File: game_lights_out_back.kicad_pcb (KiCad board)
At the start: 2 copper layers, 171 x 131.3 mm, 6 parts

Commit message: Added game legend
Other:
- board text added: "EASY"
- board text added: "HARD"
- board text added: "MAD"
- board text added: "MODE"
- board text added: "PATTERN"
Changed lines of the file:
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@@
     (pad "1" thru_hole circle (at 0 0) (size 5.6 5.6) (drill 3.2) (layers "*.Cu" "*.Mask"))
   )
+  (gr_circle (center 90.543571 118.5) (end 88.718571 119.325)
+    (stroke (width 0.32) (type default)) (fill none) (layer "B.SilkS"))
+  (gr_circle (center 70.6525 124.8) (end 69.8275 122.975)
+    (stroke (width 0.32) (type default)) (fill solid) (layer "B.SilkS"))
+  (gr_circle (center 99.787166 95.025) (end 97.962166 95.85)
+    (stroke (width 0.32) (type default)) (fill none) (layer "B.SilkS"))
+  (gr_circle (center 135.634643 118.5) (end 134.809643 116.675)
+    (stroke (width 0.32) (type default)) (fill solid) (layer "B.SilkS"))
+  (gr_circle (center 123.034643 124.8) (end 121.209643 125.625)
+    (stroke (width 0.32) (type default)) (fill none) (layer "B.SilkS"))
+  (gr_circle (center 93.814976 95.025) (end 91.989976 95.85)
+    (stroke (width 0.15) (type default)) (fill solid) (layer "B.SilkS"))
+  (gr_circle (center 96.843571 118.5) (end 95.018571 119.325)
+    (stroke (width 0.32) (type default)) (fill solid) (layer "B.SilkS"))
+  (gr_circle (center 58.0525 112.2) (end 56.2275 113.025)
+    (stroke (width 0.32) (type default)) (fill solid) (layer "B.SilkS"))
+  (gr_circle (center 64.3525 124.8) (end 62.5275 125.625)
+    (stroke (width 0.32) (type default)) (fill none) (layer "B.SilkS"))
+  (gr_circle (center 61.366405 95.11) (end 59.541405 95.935)
+    (stroke (width 0.15) (type default)) (fill solid) (layer "B.SilkS"))
+  (gr_circle (center 129.334643 124.8) (end 127.509643 125.625)
+    (stroke (width 0.32) (type default)) (fill none) (layer "B.SilkS"))
+  (gr_circle (center 103.143571 124.8) (end 102.318571 122.975)
+    (stroke (width 0.32) (type default)) (fill solid) (layer "B.SilkS"))
+  (gr_line (start 176.7175 106.025) (end 49.5025 106.025)
+    (stroke (width 0.15) (type default)) (layer "B.SilkS"))
+  (gr_circle (center 58.0525 118.5) (end 56.2275 119.325)
+    (stroke (width 0.32) (type default)) (fill none) (layer "B.SilkS"))
+  (gr_circle (center 132.363238 95.025) (end 130.538238 95.85)
+    (stroke (width 0.15) (type default)) (fill solid) (layer "B.SilkS"))
+  (gr_circle (center 129.334643 112.2) (end 127.509643 113.025)
+    (stroke (width 0.32) (type default)) (fill none) (layer "B.SilkS"))
+  (gr_circle (center 90.543571 112.2) (end 88.718571 113.025)
+    (stroke (width 0.32) (type default)) (fill solid) (layer "B.SilkS"))
+  (gr_circle (center 90.543571 124.8) (end 88.718571 125.625)
+    (stroke (width 0.32) (type default)) (fill solid) (layer "B.SilkS"))
+  (gr_circle (center 96.843571 112.2) (end 95.018571 113.025)
+    (stroke (width 0.32) (type default)) (fill none) (layer "B.SilkS"))
+  (gr_circle (center 64.3525 118.5) (end 62.5275 119.325)
+    (stroke (width 0.32) (type default)) (fill solid) (layer "B.SilkS"))
+  (gr_line (start 143.7275 83.6) (end 143.7275 128.625)
+    (stroke (width 0.15) (type default)) (layer "B.SilkS"))
+  (gr_circle (center 64.3525 112.2) (end 62.5275 113.025)
+    (stroke (width 0.32) (type default)) (fill none) (layer "B.SilkS"))
+  (gr_circle (center 70.6525 112.2) (end 69.8275 110.375)
+    (stroke (width 0.32) (type default)) (fill none) (layer "B.SilkS"))
+  (gr_circle (center 123.034643 118.5) (end 121.209643 119.325)
+    (stroke (width 0.32) (type default)) (fill solid) (layer "B.SilkS"))
+  (gr_line (start 113.11 83.5125) (end 113.11 128.5375)
+    (stroke (width 0.15) (type default)) (layer "B.SilkS"))
+  (gr_circle (center 135.634643 124.8) (end 134.809643 122.975)
+    (stroke (width 0.32) (type default)) (fill none) (layer "B.SilkS"))
+  (gr_circle (center 103.143571 112.2) (end 102.318571 110.375)
+    (stroke (width 0.32) (type default)) (fill solid) (layer "B.SilkS"))
+  (gr_circle (center 96.843571 124.8) (end 95.018571 125.625)
+    (stroke (width 0.32) (type default)) (fill none) (layer "B.SilkS"))
+  (gr_circle (center 123.034643 112.2) (end 121.209643 113.025)
+    (stroke (width 0.32) (type default)) (fill none) (layer "B.SilkS"))
+  (gr_circle (center 103.143571 118.5) (end 102.318571 116.675)
+    (stroke (width 0.32) (type default)) (fill none) (layer "B.SilkS"))
+  (gr_circle (center 58.0525 124.8) (end 56.2275 125.625)
+    (stroke (width 0.32) (type default)) (fill solid) (layer "B.SilkS"))
+  (gr_line (start 80.0775 83.6875) (end 80.0775 128.7125)
+    (stroke (width 0.15) (type default)) (layer "B.SilkS"))
+  (gr_circle (center 135.634643 112.2) (end 134.809643 110.375)
+    (stroke (width 0.32) (type default)) (fill none) (layer "B.SilkS"))
+  (gr_circle (center 126.391048 95.025) (end 124.566048 95.85)
+    (stroke (width 0.32) (type default)) (fill none) (layer "B.SilkS"))
+  (gr_circle (center 129.334643 118.5) (end 127.509643 119.325)
+    (stroke (width 0.32) (type default)) (fill solid) (layer "B.SilkS"))
+  (gr_circle (center 70.6525 118.5) (end 69.8275 116.675)
+    (stroke (width 0.32) (type default)) (fill solid) (layer "B.SilkS"))
+  (gr_circle (center 67.338595 95.11) (end 65.513595 95.935)
+    (stroke (width 0.15) (type default)) (fill solid) (layer "B.SilkS"))
   (gr_line (start 198.5 36.225) (end 198.5 159.727959)
     (stroke (width 0.15) (type default)) (layer "Edge.Cuts"))
@@
   (gr_line (start 180.25 163.6) (end 180.25 156.182741)
     (stroke (width 0.15) (type default)) (layer "Edge.Cuts"))
+  (gr_text "PATTERN" (at 176.4525 120.825) (layer "B.SilkS")
+    (effects (font (size 4 4) (thickness 0.4)) (justify left bottom mirror))
+  )
+  (gr_text "HARD" (at 103.000714 90.525) (layer "B.SilkS")
+    (effects (font (size 3 3) (thickness 0.4)) (justify left bottom mirror))
+  )
+  (gr_text "MODE" (at 167.50012 94.25) (layer "B.SilkS")
+    (effects (font (size 4 4) (thickness 0.4)) (justify left bottom mirror))
+  )
+  (gr_text "EASY" (at 134.991787 90.525) (layer "B.SilkS")
+    (effects (font (size 3 3) (thickness 0.4)) (justify left bottom mirror))
+  )
+  (gr_text "MAD" (at 69.1525 90.525) (layer "B.SilkS")
+    (effects (font (size 3 3) (thickness 0.4)) (justify left bottom mirror))
+  )
+  (group "" (id 455a1178-df87-44ea-8b91-7235553cbc28)
+    (members
+      261d7f8f-eeb7-481b-b0fd-0129d406c052
+      31291336-dc73-473a-90ed-17b8841096d2
+      712f0788-e002-4239-ad1e-24f4e175bcd2
+      8e6f98e7-f303-4edb-9ed7-cce28ad63303
+      be6bbd4a-08f9-4030-81eb-1beb07f88b7c
+      c17f5380-33c9-43a8-ab61-9f4c6e177f09
+      d1aa2f9a-0e7d-41fc-bcbe-736c27e86cbd
+      eb4e7400-9f0f-4575-ad00-f8157b8538a5
+      f5d11564-91a7-4068-9d18-078f88d7d862
+    )
+  )
+  (group "" (id 4dc2f626-c3d2-4060-a3be-768ad604da2b)
+    (members
+      07da0751-2c31-44d3-99a5-5aa53a375bff
+      438c2c47-9fb8-4051-8d9e-e72ad2a0274b
+      76975fe7-c488-4ce5-bf1f-eac8981398e5
+      a54ff637-b3a6-470e-a70b-c42ad9011c36
+      ae910db0-71ba-44e7-88aa-81bdfe88f295
+      aef7c534-f206-4ee9-8209-9a302de551d4
+      c1805144-67f5-4b0d-a860-4b305fad90ab
+      cb096a48-ffeb-4345-9da1-fc4f11216af2
+      d496f436-2d81-4b0a-bf6d-a08bfc9afeff
+    )
+  )
+  (group "" (id 61e4d897-ca6c-446e-94a5-61c08a7e7259)
+    (members
+      8bbff44d-510c-48ff-aa89-9c50f5b69c16
+      ee6aea0f-4c68-45f7-ae33-8406a4bfbe19
+    )
+  )
+  (group "" (id 67464c34-3e7d-40d0-be52-a913a4eaf996)
+    (members
+      2339e411-381a-4944-9f1f-b95e121b9fc1
+      3168bb83-6634-49cf-ad96-58e831066aa5
+    )
+  )
+  (group "" (id 80c131fc-5c4e-43d1-8e09-e49daf85af34)
+    (members
+      455a1178-df87-44ea-8b91-7235553cbc28
+      61e4d897-ca6c-446e-94a5-61c08a7e7259
+      c3cd3924-3d74-4e30-ab55-2307731a8833
+    )
+  )
+  (group "" (id 91758048-96f1-479b-bb8d-28c89c69f6ab)
+    (members
+      14b17e3b-d8df-4574-a00d-e5d4e06a5459
+      4ce1c812-a6f5-45a7-b9a3-cad09bde9c3c
+      54570bfe-5cb2-40cf-a7d2-30e87427faab
+      820d155b-5a26-4ab3-92a4-9c2c56f77b37
+      b3fc83cb-e340-4e87-9f77-882285466c1f
+      b9e060ff-2673-433b-830e-2caefa8c77f6
+      bc24d5b1-d3ef-45bb-aa2a-21220477ee76
+      d9833f43-baa8-45ae-955f-11ed89836e60
+      f8c12218-be2d-4702-add2-c302c442c423
+    )
+  )
+  (group "" (id b6545c7e-3622-4671-9b87-6c9b06a56718)
+    (members
+      6c75ff73-f754-43bb-91ea-8040bd60d2ff
+      fbe0b7d8-f2e1-4739-a7ad-3f0e8ba8aecb
+    )
+  )
+  (group "" (id d41bcf04-e3df-4054-a65c-2d4ca95d018d)
+    (members
+      91758048-96f1-479b-bb8d-28c89c69f6ab
+      b6545c7e-3622-4671-9b87-6c9b06a56718
+      fba90e10-5910-4907-8e2a-2ec4c74c6d5b
+    )
+  )
+  (group "" (id ec3535d2-e539-4bf3-b8bf-7634c9ccf21e)
+    (members
+      12a2a039-d112-4518-9f0d-b386f7ff85a5
+      4dc2f626-c3d2-4060-a3be-768ad604da2b
+      67464c34-3e7d-40d0-be52-a913a4eaf996
+    )
+  )
+  (group "" (id fcbf9672-2996-4a34-a5b4-5728ca826a9f)
+    (members
+      0037a36e-4962-436a-989b-bd0749ca4518
+      803bd84f-acab-4c13-87fe-f79ba7d896b0
+      80c131fc-5c4e-43d1-8e09-e49daf85af34
+      a7b7fe95-01c0-41a5-bf3d-10d29c617146
+      b6bcb3e3-351b-4e05-babd-601cb4178a56
+      bfb116fe-4cda-4710-86c5-b7c981d3c595
+      d41bcf04-e3df-4054-a65c-2d4ca95d018d
+      dcec1135-b45b-405c-926b-d7de8021f556
+      ec3535d2-e539-4bf3-b8bf-7634c9ccf21e
+    )
+  )
 )

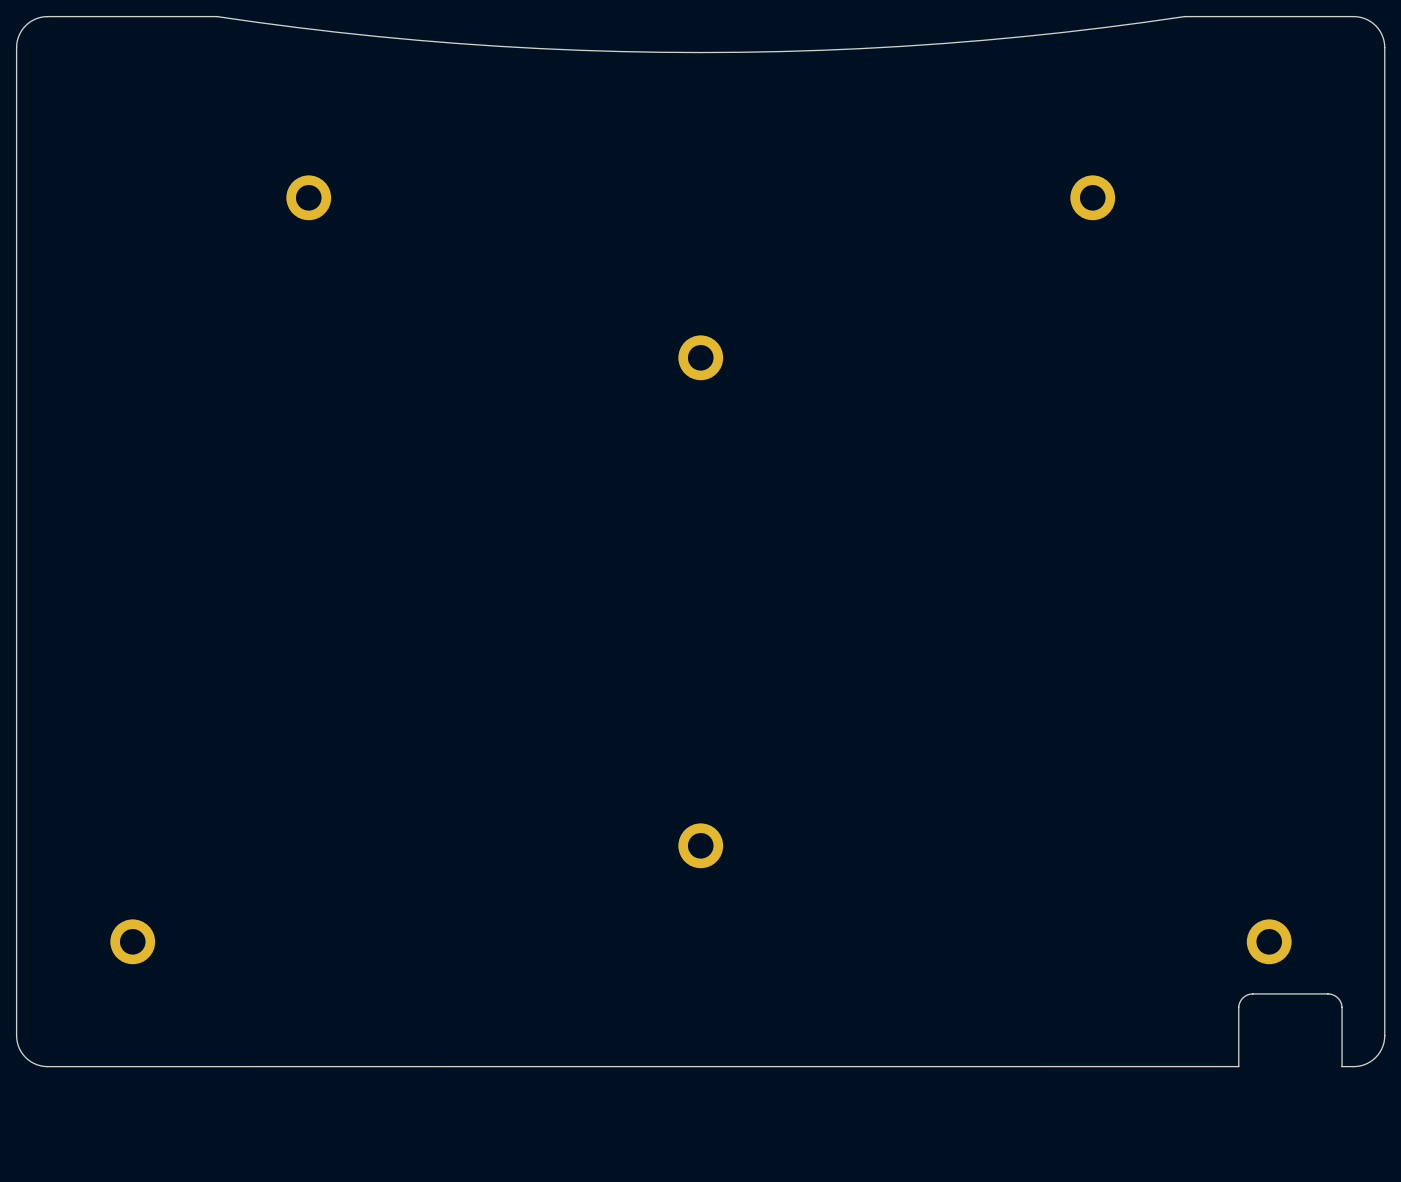
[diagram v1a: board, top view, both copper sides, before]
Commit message: Updated mounting holes
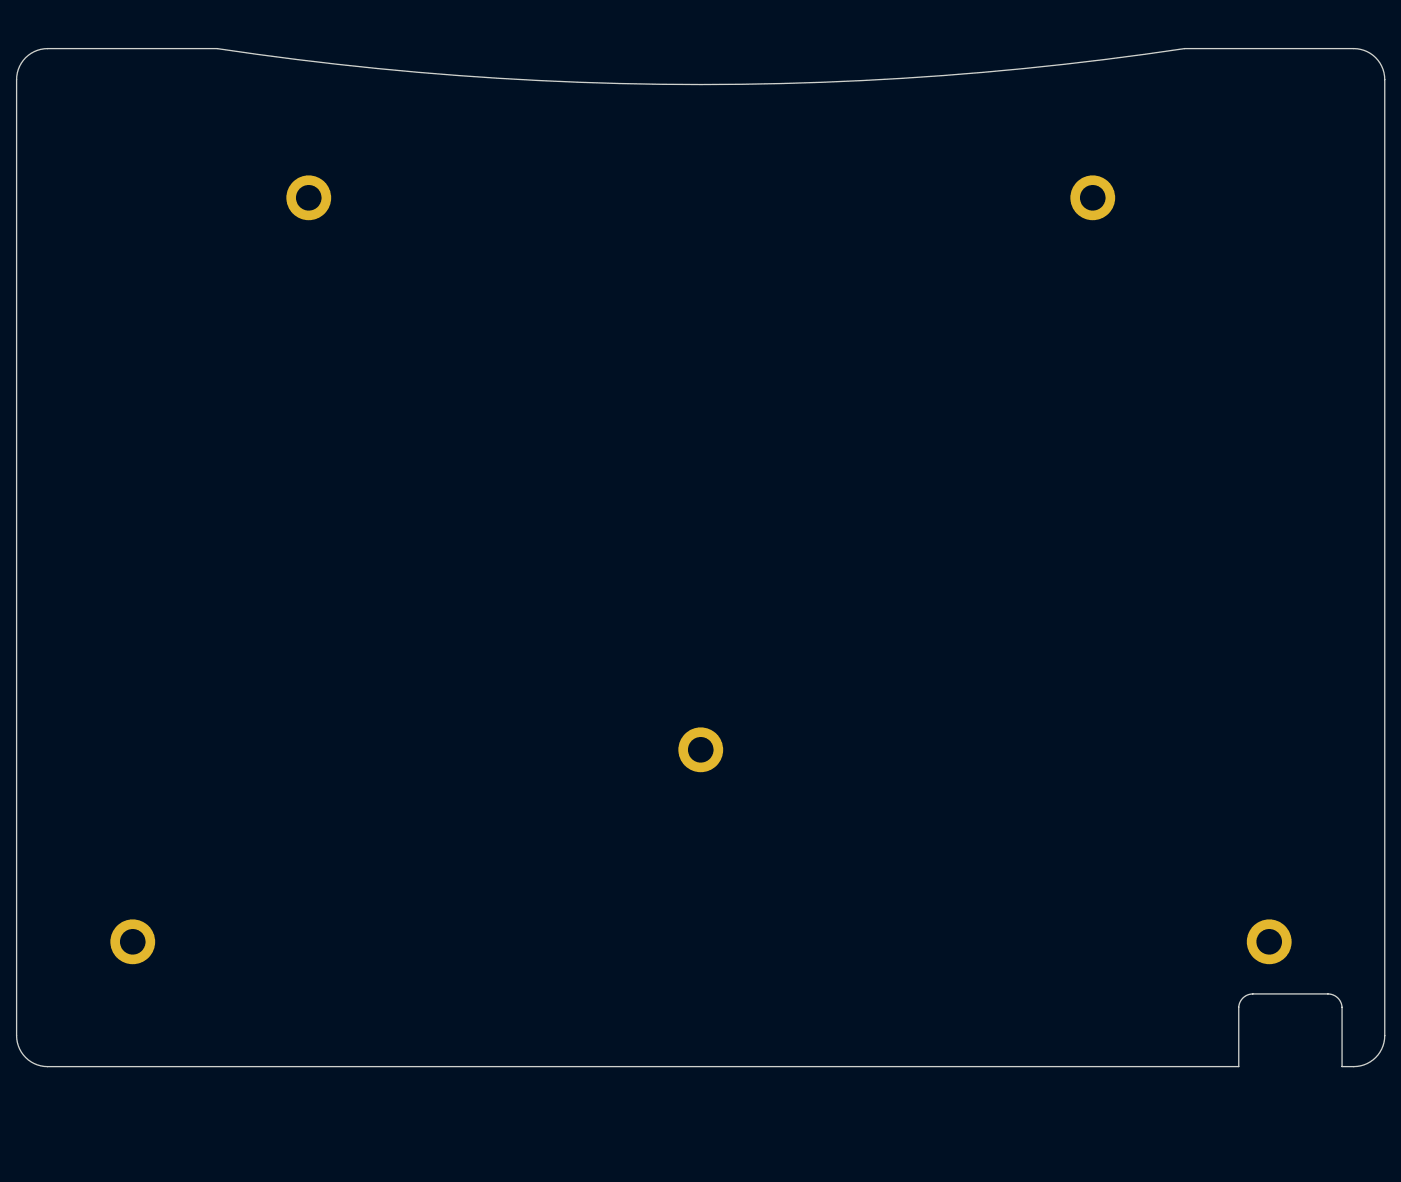
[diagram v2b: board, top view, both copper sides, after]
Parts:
- removed the REF** at (113.0, 136.0)
- moved REF** 49.0 mm to (113.0, 124.0)
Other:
- board size 171 x 131.3 mm -> 171 x 127.3 mm

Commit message: Finilized decorations
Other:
- board text added: "ΓΙΑ ΤΗ ΝΙΚΗ ΚΑΙ ΤΟΝ ΚΩΣΤΑ"
